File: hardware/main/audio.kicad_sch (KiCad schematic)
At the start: 30 parts, among them U2 PCM5122PW, U3 PAM8406DR, U4 ICS-43434

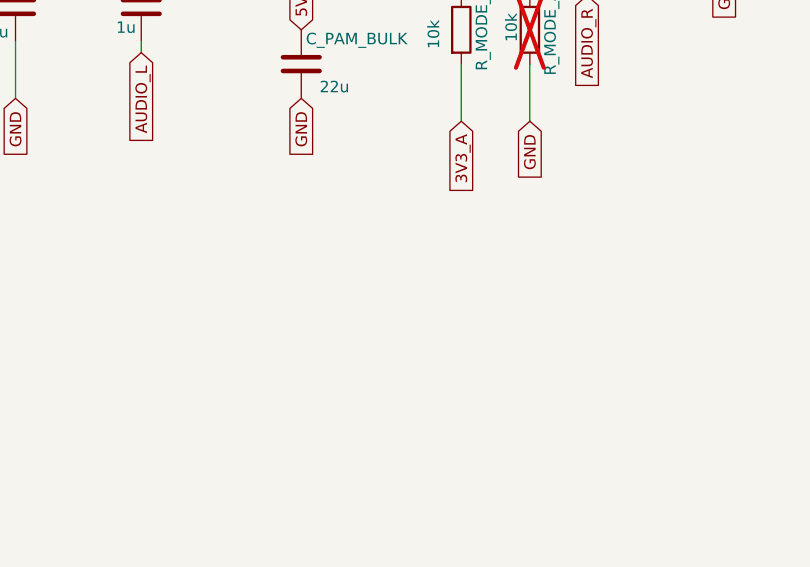
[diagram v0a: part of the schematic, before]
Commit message: hardware(audio): connecteur haut-parleur J10 + ferrites FB3-FB6
Solde le dernier point bloquant de l'audit 2026-09-23 (A2) : HP_L+/-, HP_R+/-
n'aboutissaient a aucun connecteur.

Schema (feuille audio, zone verifiee libre) :
  U3.OUT -> HP_x -> FB3..FB6 -> SPK_x -> J10.1..4
- J10 : JST PH 4 broches (1 = L+, 2 = L-, 3 = R+, 4 = R-), meme famille que J9.
  Sorties en pont : aucune masse commune, les "-" ne doivent jamais etre reliees
  entre elles ni a GND (note portee dans le champ Description du symbole).
- FB3-FB6 : Murata BLM21PG221SN1D, une ferrite par fil, exigee par la datasheet
  PAM8406 en classe D sans filtre (Application Note 2). 220 ohm a 100 MHz, 2 A a
  85 C, 45 mOhm, LCSC C85840. Le courant reel est 0,47 A rms / 0,67 A crete.
  /!\ Les series BLM21BB/BD/RK de meme impedance ne tiennent que 200-600 mA :
  elles auraient grille. Piege documente dans la fiche.
Verifie par tools/kicad_netlist.py : 12 pins ajoutees, 12 raccordees.
Reste a faire cote KiCad : ouvrir la feuille audio et lancer l'ERC (le bloc est
insere par script, electriquement juste, rendu a valider visuellement).

Haut-parleur retenu : PUI Audio AS04008PO-2-R, 8 ohm, 1 W nominal / 2 W max.
Le PDF se contredit (page 1 : 2 W/4 W ; tableau du dessin cote : 1 W/2 W) ;
c'est le tableau qui fait foi, la fiche produit le confirme. Consequences :
- l'ampli plafonne a 1,8 W sur 8 Ω, donc sous le max du HP -> pas de risque,
- mais au-dessus de son 1 W nominal -> plafond de volume a -22 dB (et non -20),
- le rail 5 V ne prend plus que ~0,4 A par canal au lieu de 1,15-1,44 A en 4 Ω,
  ce qui detend le budget du boost et de D1.

Nouvelles fiches datasheets : BLM21PG.md, AS04008PO.md (+ PDF officiels).
tools/pdf_text.py : decodage des polices a encodage propriétaire (tables
/ToUnicode et /Differences par noms de glyphes) — sans ca la datasheet PUI
sortait en charabia et la contradiction 1 W / 2 W serait passee inapercue.

Co-Authored-By: Claude Opus 5 <noreply@anthropic.com>
Claude-Session: https://claude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
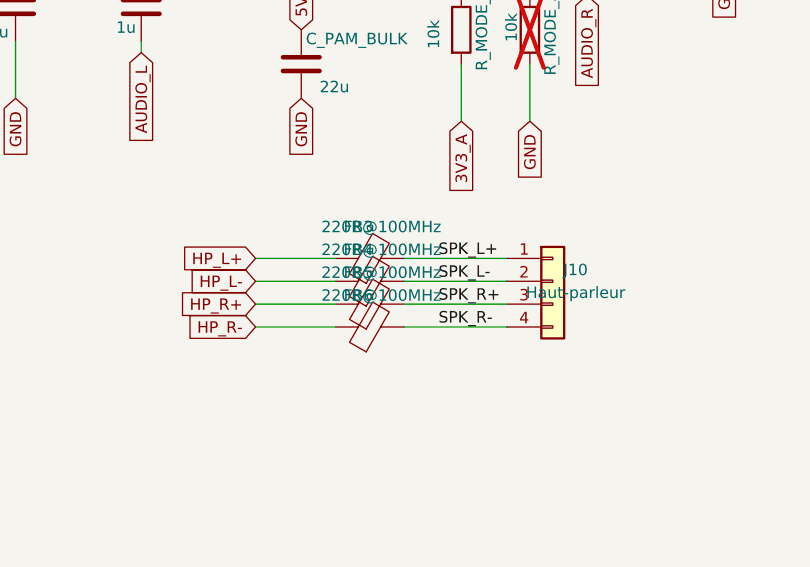
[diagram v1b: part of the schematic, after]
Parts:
- added FB3, FB4, FB5, FB6: 220R@100MHz, Inductor_SMD:L_0805_2012Metric, symbol Device:FerriteBead
- added J10: Haut-parleur, Connector_JST:JST_PH_B4B-PH-K_1x04-P2.00mm_Vertical, symbol Connector_Generic:Conn_01x04
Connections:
- net HP_L+: now also FB3.1
- net HP_L-: now also FB4.1
- net HP_R+: now also FB5.1
- net HP_R-: now also FB6.1
- new net SPK_L+: FB3.2, J10.1 (Pin_1)
- new net SPK_L-: FB4.2, J10.2 (Pin_2)
- new net SPK_R+: FB5.2, J10.3 (Pin_3)
- new net SPK_R-: FB6.2, J10.4 (Pin_4)
